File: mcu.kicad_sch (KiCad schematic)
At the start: 11 parts, among them J301 Conn_01x07_Pin, J302 Conn_01x07_Pin, SW301 TS-1088R-02026, SW302 TS-1088R-02026, U301 ESP-12F

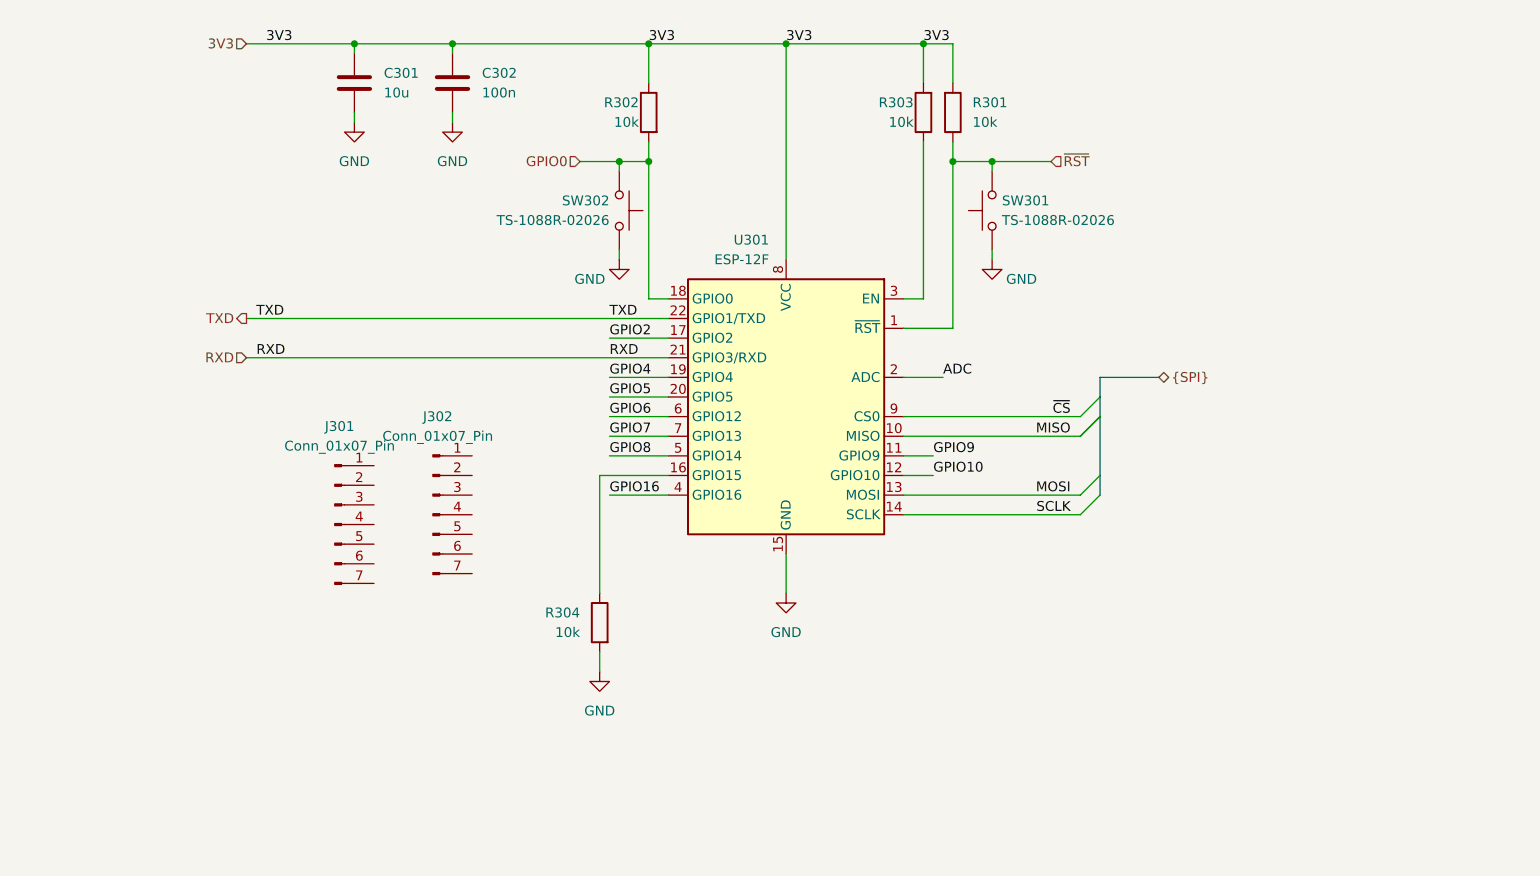
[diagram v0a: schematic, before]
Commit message: Switch to 16 pin USB-C
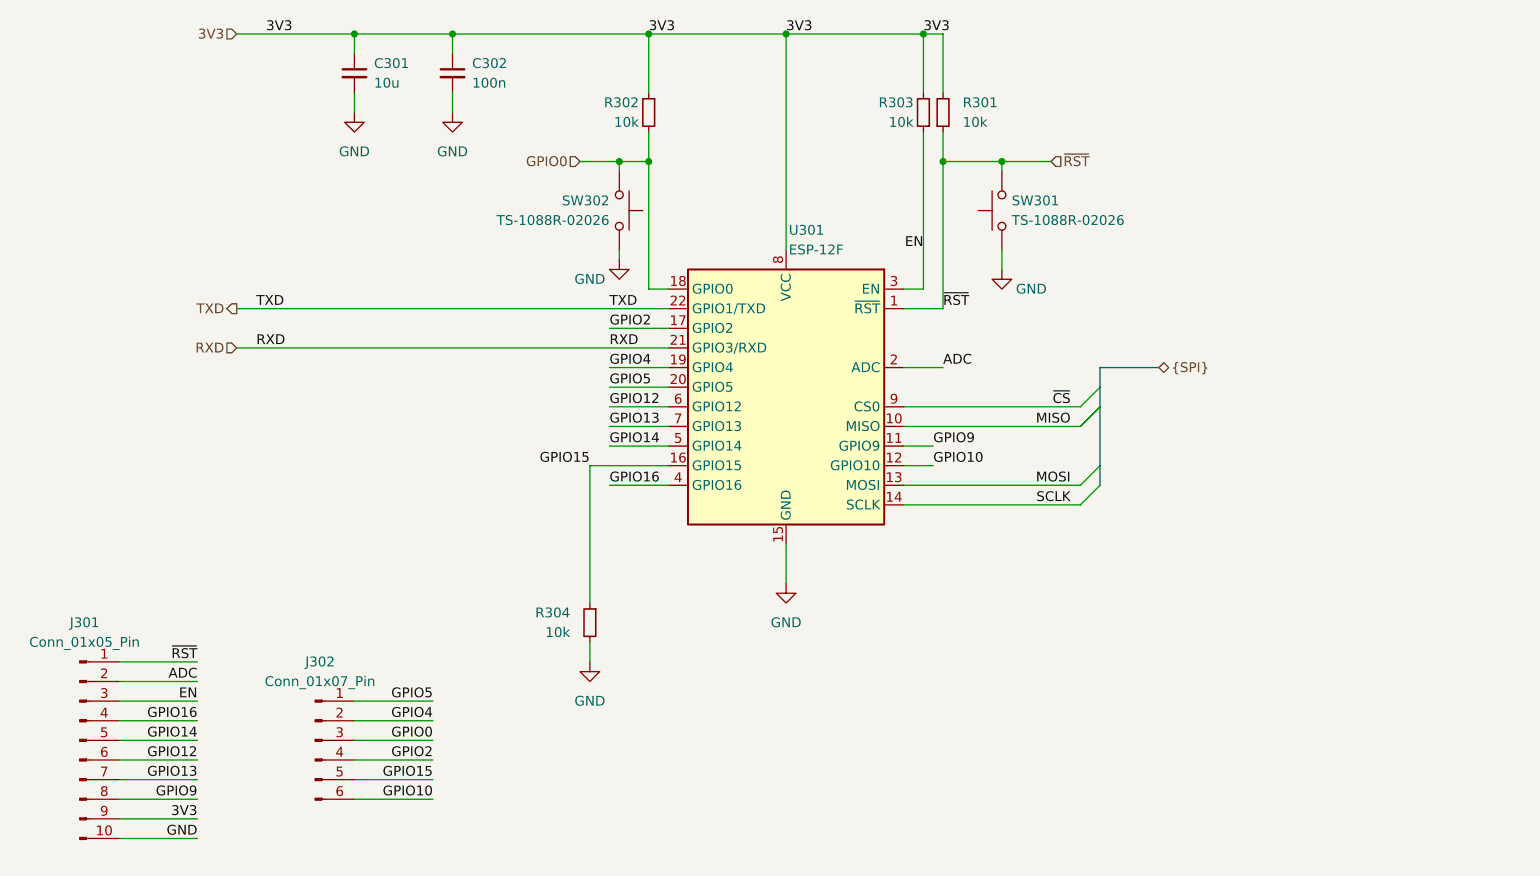
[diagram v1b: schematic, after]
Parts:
- removed U301: ESP-12F, RF_Module:ESP-12E, symbol RF_Module:ESP-12F
- added U301: ESP-12F, RF_Module:ESP-12E, symbol busbuddy:ESP-12F
- C301, C302: symbol Device:C -> Device:C_Small
- J301: value Conn_01x07_Pin -> Conn_01x05_Pin; footprint Connector_PinHeader_2.54mm:PinHeader_1x07_P2.54mm_Vertical -> Connector_PinHeader_2.54mm:PinHeader_1x10_P2.54mm_Vertical; symbol Connector:Conn_01x07_Pin -> Connector:Conn_01x10_Pin
- J302: footprint Connector_PinHeader_2.54mm:PinHeader_1x07_P2.54mm_Vertical -> Connector_PinHeader_2.54mm:PinHeader_1x06_P2.54mm_Vertical; symbol Connector:Conn_01x07_Pin -> Connector:Conn_01x06_Pin
- R301, R302, R303, R304: symbol Device:R -> Device:R_Small
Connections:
- net 3V3: now also J301.9 (Pin_9), U301.8 (VCC)
- net ADC: now also J301.2 (Pin_2), U301.2 (ADC)
- net GND: now also J301.10 (Pin_10), U301.15 (GND)
- net GPIO0: now also J302.3 (Pin_3), U301.18 (GPIO0)
- net GPIO10: now also J302.6 (Pin_6), U301.12 (GPIO10)
- net GPIO16: now also J301.4 (Pin_4), U301.4 (GPIO16)
- net GPIO2: now also J302.4 (Pin_4), U301.17 (GPIO2)
- net GPIO4: now also J302.2 (Pin_2), U301.19 (GPIO4)
- net GPIO5: now also J302.1 (Pin_1), U301.20 (GPIO5)
- net GPIO9: now also J301.8 (Pin_8), U301.11 (GPIO9)
- net MISO: now also U301.10 (MISO)
- net MOSI: now also U301.13 (MOSI)
- net RXD: now also U301.21 (GPIO3/RXD)
- net SCLK: now also U301.14 (SCLK)
- net TXD: now also U301.22 (GPIO1/TXD)
- net ~{CS}: now also U301.9 (CS0)
- net ~{RST}: now also J301.1 (Pin_1), U301.1 (~{RST})
- net GPIO15: now reaches R304.1
- net GPIO15: now also J302.5 (Pin_5), U301.16 (GPIO15)
- net EN: now reaches R303.1
- net EN: now also J301.3 (Pin_3), U301.3 (EN)
- net GPIO14: now reaches J301.5 (Pin_5)
- net GPIO14: now also U301.5 (GPIO14)
- net GPIO12: now reaches J301.6 (Pin_6)
- net GPIO12: now also U301.6 (GPIO12)
- net GPIO13: now reaches J301.7 (Pin_7)
- net GPIO13: now also U301.7 (GPIO13)
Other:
- moved on the sheet: C301, C302, R301, R304, SW301

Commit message: Correct SPI pinout
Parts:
- J302: value Conn_01x07_Pin -> Conn_01x10_Pin; footprint Connector_PinHeader_2.54mm:PinHeader_1x06_P2.54mm_Vertical -> Connector_PinHeader_2.54mm:PinHeader_1x10_P2.54mm_Vertical; symbol Connector:Conn_01x06_Pin -> Connector:Conn_01x10_Pin
- U301: LCSC Part Number (none) -> C82891; MPN (none) -> ESP-12F(ESP8266MOD); Manufacturer (none) -> Ai-Thinker
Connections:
- net MISO: now also J302.8 (Pin_8)
- net MOSI: now also J302.9 (Pin_9)
- net SCLK: now also J302.10 (Pin_10)
- net GPIO0 renamed EPD_D/C
- net GPIO13 renamed SPI.MOSI
- net GPIO14 renamed SPI.SCLK
- net GPIO15 renamed SPI.~{CS}
- net GPIO2 renamed EPD_RST
- net GPIO4 renamed EPD_BUSY
- net ~{CS} renamed CS0
- net CS0: now also J302.7 (Pin_7)
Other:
- note added: "GPIO13"
- note added: "GPIO14"
- note added: "GPIO15"

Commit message: Finish everything
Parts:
- J301: footprint Connector_PinHeader_2.54mm:PinHeader_1x10_P2.54mm_Vertical -> Connector_PinHeader_2.54mm:PinHeader_1x12_P2.54mm_Vertical; symbol Connector:Conn_01x10_Pin -> Connector:Conn_01x12_Pin; now left out of the parts list
- J302: now left out of the parts list
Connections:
- net 3V3: now also J301.8 (Pin_8); no longer J301.9 (Pin_9)
- net CS0: now also J301.10 (Pin_10); no longer J302.7 (Pin_7)
- net EPD_BUSY: now also J302.4 (Pin_4); no longer J302.2 (Pin_2)
- net EPD_D/C: now also J302.6 (Pin_6); no longer J302.3 (Pin_3)
- net EPD_RST: now also J302.5 (Pin_5); no longer J302.4 (Pin_4)
- net GND: now also J301.9 (Pin_9); no longer J301.10 (Pin_10)
- net GPIO10: now also J302.10 (Pin_10); no longer J302.6 (Pin_6)
- net GPIO12: now also J301.5 (Pin_5); no longer J301.6 (Pin_6)
- net GPIO5: now also J302.3 (Pin_3); no longer J302.1 (Pin_1)
- net GPIO9: now also J301.12 (Pin_12); no longer J301.8 (Pin_8)
- net MISO: now also J301.11 (Pin_11); no longer J302.8 (Pin_8)
- net RXD: now also J302.2 (Pin_2)
- net SCLK: now also J302.8 (Pin_8); no longer J302.10 (Pin_10)
- net SPI.MOSI: now also J301.6 (Pin_6); no longer J301.7 (Pin_7)
- net SPI.SCLK: now also J301.7 (Pin_7); no longer J301.5 (Pin_5)
- net SPI.~{CS}: now also J302.7 (Pin_7); no longer J302.5 (Pin_5)
- net TXD: now also J302.1 (Pin_1)
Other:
- note added: "GPIO1"
- note added: "GPIO3"

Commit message: Rename project
Damn squatters
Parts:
- SW301, SW302: footprint busbuddy:TS-1088R-02026_SW_SMD_3x4mm -> youdbetterrun:TS-1088R-02026_SW_SMD_3x4mm
- U301: symbol busbuddy:ESP-12F -> youdbetterrun:ESP-12F
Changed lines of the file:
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@@
 		)
 		(instances
-			(project "busbuddy"
+			(project "youdbetterrun"
 				(path "/50da2b4e-34b1-4787-8ee6-5d7d17f804f4/81f185f6-8abd-42b2-b2d9-f7e00f67ab8b"
 					(reference "#PWR0304")
@@
 		)
 		(instances
-			(project "busbuddy"
+			(project "youdbetterrun"
 				(path "/50da2b4e-34b1-4787-8ee6-5d7d17f804f4/81f185f6-8abd-42b2-b2d9-f7e00f67ab8b"
 					(reference "#PWR0309")
@@
 		)
 		(instances
-			(project "busbuddy"
+			(project "youdbetterrun"
 				(path "/50da2b4e-34b1-4787-8ee6-5d7d17f804f4/81f185f6-8abd-42b2-b2d9-f7e00f67ab8b"
 					(reference "C302")
@@
 		)
 		(instances
-			(project "busbuddy"
+			(project "youdbetterrun"
 				(path "/50da2b4e-34b1-4787-8ee6-5d7d17f804f4/81f185f6-8abd-42b2-b2d9-f7e00f67ab8b"
 					(reference "C301")
@@
 		)
 		(instances
-			(project "busbuddy"
+			(project "youdbetterrun"
 				(path "/50da2b4e-34b1-4787-8ee6-5d7d17f804f4/81f185f6-8abd-42b2-b2d9-f7e00f67ab8b"
 					(reference "#PWR0308")
@@
 		)
 		(instances
-			(project "busbuddy"
+			(project "youdbetterrun"
 				(path "/50da2b4e-34b1-4787-8ee6-5d7d17f804f4/81f185f6-8abd-42b2-b2d9-f7e00f67ab8b"
 					(reference "J302")
@@
 		)
 		(instances
-			(project "busbuddy"
+			(project "youdbetterrun"
 				(path "/50da2b4e-34b1-4787-8ee6-5d7d17f804f4/81f185f6-8abd-42b2-b2d9-f7e00f67ab8b"
 					(reference "J301")
@@
 		)
 		(instances
-			(project "busbuddy"
+			(project "youdbetterrun"
 				(path "/50da2b4e-34b1-4787-8ee6-5d7d17f804f4/81f185f6-8abd-42b2-b2d9-f7e00f67ab8b"
 					(reference "R304")
@@
 		)
 		(instances
-			(project "busbuddy"
+			(project "youdbetterrun"
 				(path "/50da2b4e-34b1-4787-8ee6-5d7d17f804f4/81f185f6-8abd-42b2-b2d9-f7e00f67ab8b"
 					(reference "#PWR0303")
@@
 		)
 		(instances
-			(project "busbuddy"
+			(project "youdbetterrun"
 				(path "/50da2b4e-34b1-4787-8ee6-5d7d17f804f4/81f185f6-8abd-42b2-b2d9-f7e00f67ab8b"
 					(reference "R302")
@@
 		)
 		(instances
-			(project "busbuddy"
+			(project "youdbetterrun"
 				(path "/50da2b4e-34b1-4787-8ee6-5d7d17f804f4/81f185f6-8abd-42b2-b2d9-f7e00f67ab8b"
 					(reference "#PWR0310")
@@
 		)
 		(instances
-			(project "busbuddy"
+			(project "youdbetterrun"
 				(path "/50da2b4e-34b1-4787-8ee6-5d7d17f804f4/81f185f6-8abd-42b2-b2d9-f7e00f67ab8b"
 					(reference "#PWR0301")
@@
 		)
 		(instances
-			(project "busbuddy"
+			(project "youdbetterrun"
 				(path "/50da2b4e-34b1-4787-8ee6-5d7d17f804f4/81f185f6-8abd-42b2-b2d9-f7e00f67ab8b"
 					(reference "R303")
@@
 	)
 	(symbol
-		(lib_id "busbuddy:ESP-12F")
+		(lib_id "youdbetterrun:ESP-12F")
 		(at 160.02 104.14 0)
 		(mirror y)
@@
 		)
 		(instances
-			(project "busbuddy"
+			(project "youdbetterrun"
 				(path "/50da2b4e-34b1-4787-8ee6-5d7d17f804f4/81f185f6-8abd-42b2-b2d9-f7e00f67ab8b"
 					(reference "U301")
@@
 			)
 		)
-		(property "Footprint" "busbuddy:TS-1088R-02026_SW_SMD_3x4mm"
+		(property "Footprint" "youdbetterrun:TS-1088R-02026_SW_SMD_3x4mm"
 			(at 143.51 78.74 0)
 			(effects
@@
 		)
 		(instances
-			(project "busbuddy"
+			(project "youdbetterrun"
 				(path "/50da2b4e-34b1-4787-8ee6-5d7d17f804f4/81f185f6-8abd-42b2-b2d9-f7e00f67ab8b"
 					(reference "SW302")
@@
 		)
 		(instances
-			(project "busbuddy"
+			(project "youdbetterrun"
 				(path "/50da2b4e-34b1-4787-8ee6-5d7d17f804f4/81f185f6-8abd-42b2-b2d9-f7e00f67ab8b"
 					(reference "R301")
@@
 			)
 		)
-		(property "Footprint" "busbuddy:TS-1088R-02026_SW_SMD_3x4mm"
+		(property "Footprint" "youdbetterrun:TS-1088R-02026_SW_SMD_3x4mm"
 			(at 182.88 78.74 0)
 			(effects
@@
 		)
 		(instances
-			(project "busbuddy"
+			(project "youdbetterrun"
 				(path "/50da2b4e-34b1-4787-8ee6-5d7d17f804f4/81f185f6-8abd-42b2-b2d9-f7e00f67ab8b"
 					(reference "SW301")
